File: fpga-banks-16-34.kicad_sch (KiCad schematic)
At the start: 22 parts, among them U3002 XC7K160T-FFG676, U9002 PCA9517A_TSSOP, Y9001 Oscillator_100MHz_ASFL1

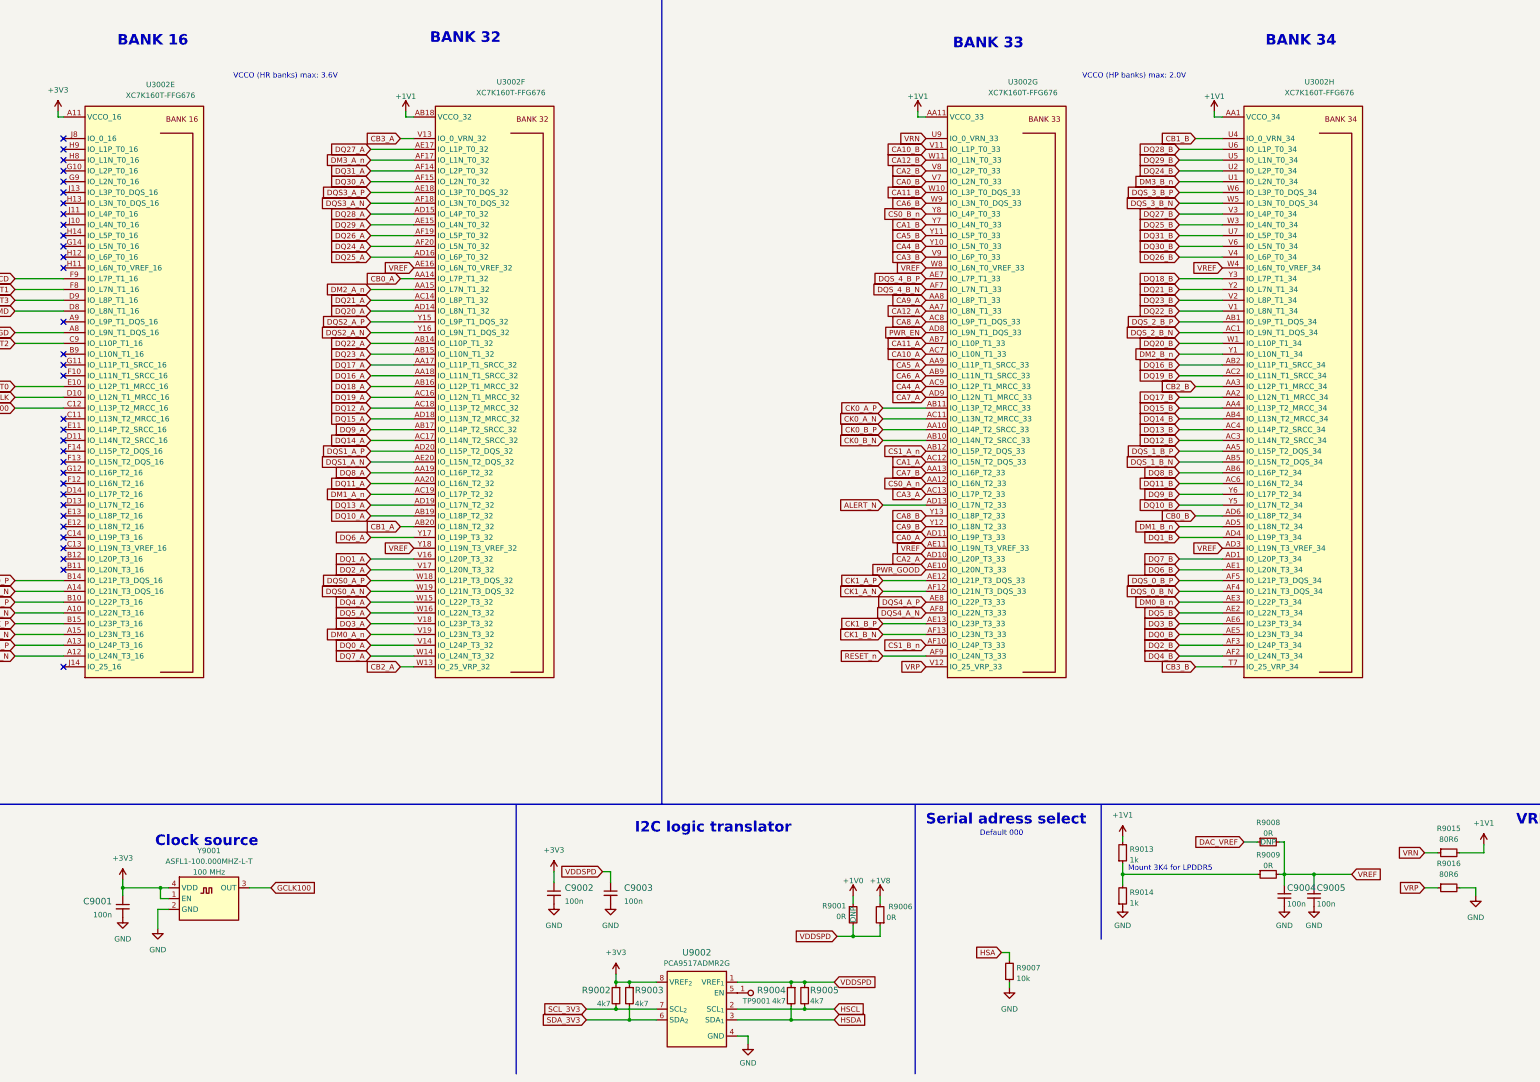
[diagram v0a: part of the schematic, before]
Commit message: Re-annotate schematic
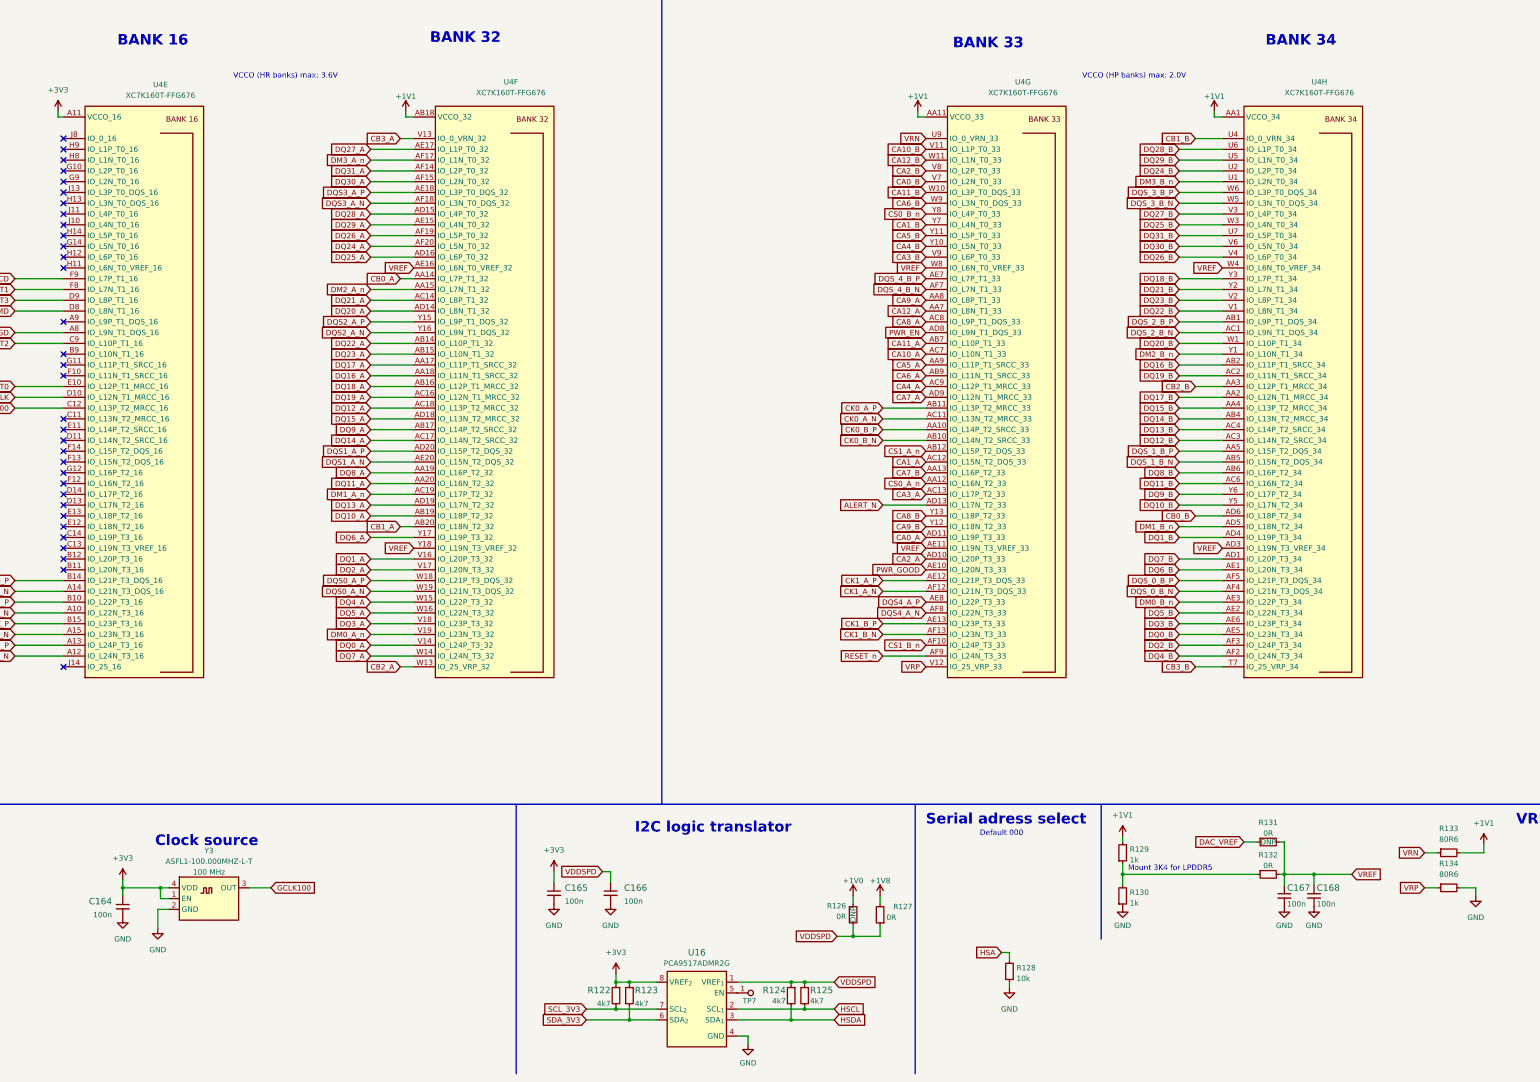
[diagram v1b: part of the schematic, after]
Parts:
- renumbered C9001 to C164, C9002 to C165, C9003 to C166, C9004 to C167, C9005 to C168, R9002 to R122, R9003 to R123, R9004 to R124, R9005 to R125, R9001 to R126, R9006 to R127, R9007 to R128, R9013 to R129, R9014 to R130, R9008 to R131, R9009 to R132, R9015 to R133, R9016 to R134, TP9001 to TP7, U9002 to U16, U3002 to U4, Y9001 to Y3

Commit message: Add local libraries
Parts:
- R129, R130: footprint antmicro-footprints:R_0402_1005Metric -> sodimm-ddr5-tester-footprints:R_0402_1005Metric; symbol antmicroResistors0402:R_1k_0402 -> sodimm-ddr5-tester:R_1k_0402
- R131, R132: footprint antmicro-footprints:R_0402_1005Metric -> sodimm-ddr5-tester-footprints:R_0402_1005Metric; symbol antmicroResistors0402:R_0R_0402 -> sodimm-ddr5-tester:R_0R_0402
- TP7: footprint antmicro-footprints:TP_SMD_1mm -> sodimm-ddr5-tester-footprints:TP_SMD_1mm; symbol antmicroTestPoints:TP_1mm_SMD -> sodimm-ddr5-tester:TP_1mm_SMD
- Y3: footprint antmicro-footprints:Oscillator_SMD_Abracon_ASFL1-4Pin_5.0x3.2mm -> sodimm-ddr5-tester-footprints:Oscillator_SMD_Abracon_ASFL1-4Pin_5.0x3.2mm; symbol antmicroOscillators:Oscillator_100MHz_ASFL1 -> sodimm-ddr5-tester:Oscillator_100MHz_ASFL1

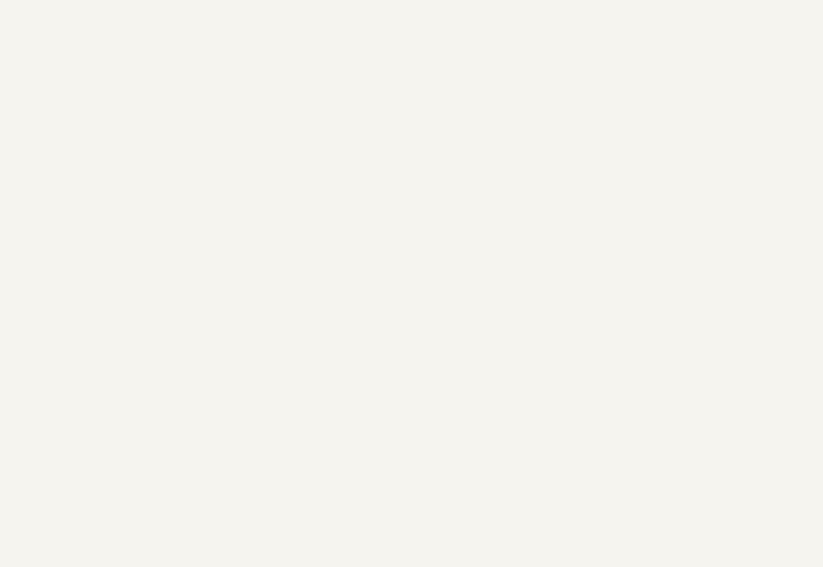
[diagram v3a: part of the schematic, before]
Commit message: Define DDR5, HyperBus and I2C buses. Connect HyperRAM with hierarchical bus
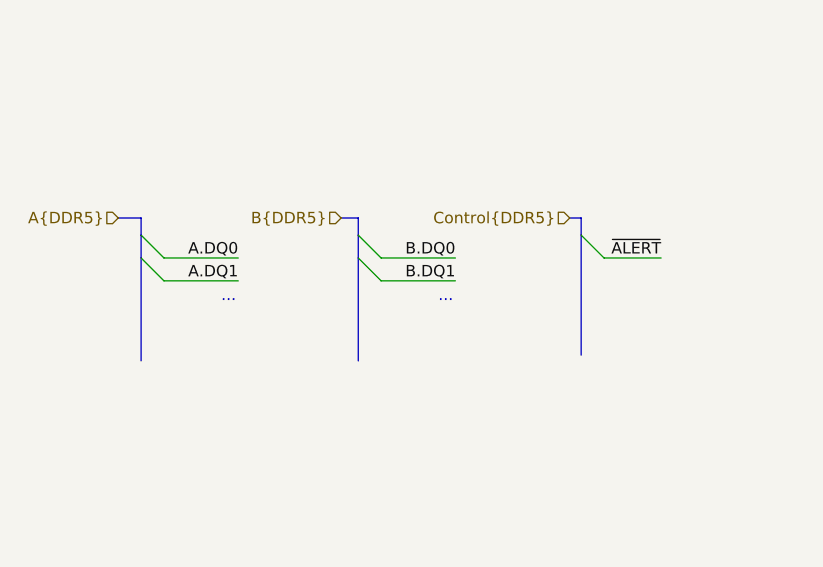
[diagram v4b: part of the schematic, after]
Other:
- note added: "..."
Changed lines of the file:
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@@
   (no_connect (at 55.88 80.01))
   (no_connect (at 55.88 148.59))
+  (bus_entry (at -13.97 136.525) (size 2.54 2.54)
+    (stroke (width 0) (type default) (color 0 0 0 0))
+  )
+  (bus_entry (at -62.865 136.525) (size 2.54 2.54)
+    (stroke (width 0) (type default) (color 0 0 0 0))
+  )
+  (bus_entry (at -38.735 136.525) (size 2.54 2.54)
+    (stroke (width 0) (type default) (color 0 0 0 0))
+  )
+  (bus_entry (at -62.865 139.065) (size 2.54 2.54)
+    (stroke (width 0) (type default) (color 0 0 0 0))
+  )
+  (bus_entry (at -38.735 139.065) (size 2.54 2.54)
+    (stroke (width 0) (type default) (color 0 0 0 0))
+  )
+  (bus (pts (xy -13.97 136.525) (xy -13.97 149.86))
+    (stroke (width 0) (type default) (color 0 0 0 0))
+  )
   (wire (pts (xy 128.27 87.63) (xy 138.43 87.63))
     (stroke (width 0) (type default) (color 0 0 0 0))
@@
     (stroke (width 0) (type default) (color 0 0 0 0))
   )
+  (bus (pts (xy -38.735 139.065) (xy -38.735 150.495))
+    (stroke (width 0) (type default) (color 0 0 0 0))
+  )
   (wire (pts (xy 384.81 241.3) (xy 388.62 241.3))
     (stroke (width 0) (type default) (color 0 0 0 0))
@@
     (stroke (width 0) (type default) (color 0 0 0 0))
   )
+  (bus (pts (xy -38.735 136.525) (xy -38.735 139.065))
+    (stroke (width 0) (type default) (color 0 0 0 0))
+  )
   (wire (pts (xy 318.77 82.55) (xy 328.93 82.55))
     (stroke (width 0) (type default) (color 0 0 0 0))
@@
     (stroke (width 0) (type default) (color 0 0 0 0))
   )
+  (bus (pts (xy -40.64 134.62) (xy -38.735 134.62))
+    (stroke (width 0) (type default) (color 0 0 0 0))
+  )
   (wire (pts (xy 44.45 128.27) (xy 55.88 128.27))
     (stroke (width 0) (type default) (color 0 0 0 0))
@@
     (stroke (width 0) (type default) (color 0 0 0 0))
   )
+  (wire (pts (xy -60.325 139.065) (xy -52.07 139.065))
+    (stroke (width 0) (type default) (color 0 0 0 0))
+  )
   (wire (pts (xy 138.43 151.13) (xy 128.27 151.13))
     (stroke (width 0) (type default) (color 0 0 0 0))
@@
     (stroke (width 0) (type default) (color 0 0 0 0))
   )
+  (bus (pts (xy -65.405 134.62) (xy -62.865 134.62))
+    (stroke (width 0) (type default) (color 0 0 0 0))
+  )
   (wire (pts (xy 318.77 148.59) (xy 328.93 148.59))
     (stroke (width 0) (type default) (color 0 0 0 0))
   )
+  (bus (pts (xy -13.97 134.62) (xy -13.97 136.525))
+    (stroke (width 0) (type default) (color 0 0 0 0))
+  )
   (wire (pts (xy 189.23 263.525) (xy 189.23 264.16))
     (stroke (width 0) (type default) (color 0 0 0 0))
@@
     (stroke (width 0) (type default) (color 0 0 0 0))
   )
+  (wire (pts (xy -11.43 139.065) (xy -5.08 139.065))
+    (stroke (width 0) (type default) (color 0 0 0 0))
+  )
   (wire (pts (xy 318.77 102.87) (xy 328.93 102.87))
     (stroke (width 0) (type default) (color 0 0 0 0))
@@
     (stroke (width 0) (type default) (color 0 0 0 0))
   )
+  (bus (pts (xy -62.865 134.62) (xy -62.865 136.525))
+    (stroke (width 0) (type default) (color 0 0 0 0))
+  )
   (wire (pts (xy 128.27 166.37) (xy 138.43 166.37))
     (stroke (width 0) (type default) (color 0 0 0 0))
@@
     (stroke (width 0) (type default) (color 0 0 0 0))
   )
+  (bus (pts (xy -62.865 136.525) (xy -62.865 139.065))
+    (stroke (width 0) (type default) (color 0 0 0 0))
+  )
   (wire (pts (xy 136.525 58.42) (xy 136.525 59.69))
     (stroke (width 0) (type default) (color 0 0 0 0))
@@
     (stroke (width 0) (type default) (color 0 0 0 0))
   )
+  (wire (pts (xy -60.325 141.605) (xy -52.07 141.605))
+    (stroke (width 0) (type default) (color 0 0 0 0))
+  )
   (wire (pts (xy 318.77 173.99) (xy 328.93 173.99))
     (stroke (width 0) (type default) (color 0 0 0 0))
@@
     (stroke (width 0) (type default) (color 0 0 0 0))
   )
+  (bus (pts (xy -38.735 134.62) (xy -38.735 136.525))
+    (stroke (width 0) (type default) (color 0 0 0 0))
+  )
   (wire (pts (xy 318.77 67.31) (xy 328.93 67.31))
     (stroke (width 0) (type default) (color 0 0 0 0))
@@
     (stroke (width 0) (type default) (color 0 0 0 0))
   )
+  (bus (pts (xy -15.24 134.62) (xy -13.97 134.62))
+    (stroke (width 0) (type default) (color 0 0 0 0))
+  )
+  (bus (pts (xy -62.865 139.065) (xy -62.865 150.495))
+    (stroke (width 0) (type default) (color 0 0 0 0))
+  )
   (wire (pts (xy 318.77 80.01) (xy 328.93 80.01))
     (stroke (width 0) (type default) (color 0 0 0 0))
   )
+  (wire (pts (xy -36.195 141.605) (xy -27.94 141.605))
+    (stroke (width 0) (type default) (color 0 0 0 0))
+  )
   (wire (pts (xy 128.27 82.55) (xy 138.43 82.55))
     (stroke (width 0) (type default) (color 0 0 0 0))
@@
     (stroke (width 0) (type default) (color 0 0 0 0))
   )
+  (wire (pts (xy -36.195 139.065) (xy -27.94 139.065))
+    (stroke (width 0) (type default) (color 0 0 0 0))
+  )
   (wire (pts (xy 69.85 241.3) (xy 78.74 241.3))
     (stroke (width 0) (type default) (color 0 0 0 0))
@@
     (effects (font (size 1.27 1.27)) (justify left bottom))
   )
+  (text "..." (at -29.845 144.145 0)
+    (effects (font (size 1.27 1.27)) (justify left bottom))
+  )
+  (text "..." (at -53.975 144.145 0)
+    (effects (font (size 1.27 1.27)) (justify left bottom))
+  )
   (text "VCCO (HP banks) max: 2.0V" (at 295.91 50.8 0)
     (effects (font (size 1.27 1.27)) (justify left bottom))
@@
     (effects (font (size 2.4892 2.4892) (thickness 0.4978) bold) (justify left bottom))
   )
+  (label "A.DQ0" (at -52.07 139.065 180)
+    (effects (font (size 1.27 1.27)) (justify right bottom))
+  )
+  (label "~{ALERT}" (at -5.08 139.065 180)
+    (effects (font (size 1.27 1.27)) (justify right bottom))
+  )
+  (label "A.DQ1" (at -52.07 141.605 180)
+    (effects (font (size 1.27 1.27)) (justify right bottom))
+  )
+  (label "B.DQ0" (at -27.94 139.065 180)
+    (effects (font (size 1.27 1.27)) (justify right bottom))
+  )
+  (label "B.DQ1" (at -27.94 141.605 180)
+    (effects (font (size 1.27 1.27)) (justify right bottom))
+  )
   (global_label "DQ20_B" (shape input) (at 318.77 113.03 180) (fields_autoplaced)
     (effects (font (size 1.27 1.27)) (justify right))
@@
     )
   )
+  (hierarchical_label "B{DDR5}" (shape input) (at -40.64 134.62 180)
+    (effects (font (size 1.27 1.27)) (justify right))
+  )
+  (hierarchical_label "A{DDR5}" (shape input) (at -65.405 134.62 180)
+    (effects (font (size 1.27 1.27)) (justify right))
+  )
+  (hierarchical_label "Control{DDR5}" (shape input) (at -15.24 134.62 180)
+    (effects (font (size 1.27 1.27)) (justify right))
+  )
   (symbol (lib_id "sodimm-ddr5-tester:PCA9517A_TSSOP") (at 214.63 263.525 0) (mirror y) (unit 1)

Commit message: Connect DDR hierarchical labels. Define and connect JTAG, RGMII, TDMS, UART, and SDIO buses. Reorganize schematic blocks between sheets
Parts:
- removed C165, C166: C_100n_0402, sodimm-ddr5-tester-footprints:C_0402_1005Metric, symbol sodimm-ddr5-tester:C_100n_0402
- removed R122, R123, R124, R125: R_4k7_0402, sodimm-ddr5-tester-footprints:R_0402_1005Metric, symbol sodimm-ddr5-tester:R_4k7_0402
- removed R126, R127: R_0R_0402, sodimm-ddr5-tester-footprints:R_0402_1005Metric, symbol sodimm-ddr5-tester:R_0R_0402
- removed R128: R_10k_0402, sodimm-ddr5-tester-footprints:R_0402_1005Metric, symbol sodimm-ddr5-tester:R_10k_0402
- removed TP7: TP_1mm_SMD, sodimm-ddr5-tester-footprints:TP_SMD_1mm, symbol sodimm-ddr5-tester:TP_1mm_SMD
- removed U16: PCA9517A_TSSOP, sodimm-ddr5-tester-footprints:TSSOP-8_3x3mm_P0.65mm, symbol sodimm-ddr5-tester:PCA9517A_TSSOP
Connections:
- net DQ0_A is gone; now on net A.DQ0: U4.V14 (IO_L24P_T3_32)
- net DQ0_B is gone; now on net B.DQ0: U4.AE5 (IO_L23N_T3_34)
- net DQ1_A is gone; now on net A.DQ1: U4.V16 (IO_L20P_T3_32)
- net DQ1_B is gone; now on net B.DQ1: U4.AD4 (IO_L19P_T3_34)
- net ALERT_N renamed Control.~{ALERT}
- net CA0_A renamed A.CA0
- net CA0_B renamed B.CA0
- net CA10_A renamed A.CA10
- net CA10_B renamed B.CA10
- net CA11_A renamed A.CA11
- net CA11_B renamed B.CA11
- net CA12_A renamed A.CA12
- net CA12_B renamed B.CA12
- net CA1_A renamed A.CA1
- net CA1_B renamed B.CA1
- net CA2_A renamed A.CA2
- net CA2_B renamed B.CA2
- net CA3_A renamed A.CA3
- net CA3_B renamed B.CA3
- net CA4_A renamed A.CA4
- net CA4_B renamed B.CA4
- net CA5_A renamed A.CA5
- net CA5_B renamed B.CA5
- net CA6_A renamed A.CA6
- net CA6_B renamed B.CA6
- net CA7_A renamed A.CA7
- net CA7_B renamed B.CA7
- net CA8_A renamed A.CA8
- net CA8_B renamed B.CA8
- net CA9_A renamed A.CA9
- net CA9_B renamed B.CA9
- net CB0_A renamed A.CB0
- net CB0_B renamed B.CB0
- net CB1_A renamed A.CB1
- net CB1_B renamed B.CB1
- net CB2_A renamed A.CB2
- net CB2_B renamed B.CB2
- net CB3_A renamed A.CB3
- net CB3_B renamed B.CB3
- net CK0_A_N renamed A.CK0_N
- net CK0_A_P renamed A.CK0_P
- net CK0_B_N renamed B.CK0_N
- net CK0_B_P renamed B.CK0_P
- net CK1_A_N renamed A.CK1_N
- net CK1_A_P renamed A.CK1_P
- net CK1_B_N renamed B.CK1_N
- net CK1_B_P renamed B.CK1_P
- net CS0_A_n renamed A.~{CS0}
- net CS0_B_n renamed B.~{CS0}
- net CS1_A_n renamed A.~{CS1}
- net CS1_B_n renamed B.~{CS1}
- net DM0_A_n renamed A.~{DM0}
- net DM0_B_n renamed B.~{DM0}
- net DM1_A_n renamed A.~{DM1}
- net DM1_B_n renamed B.~{DM1}
- net DM2_A_n renamed A.~{DM2}
- net DM2_B_n renamed B.~{DM2}
- net DM3_A_n renamed A.~{DM3}
- net DM3_B_n renamed B.~{DM3}
- net DQ10_A renamed A.DQ10
- net DQ10_B renamed B.DQ10
- net DQ11_A renamed A.DQ11
- net DQ11_B renamed B.DQ11
- net DQ12_A renamed A.DQ12
- net DQ12_B renamed B.DQ12
- net DQ13_A renamed A.DQ13
- net DQ13_B renamed B.DQ13
- net DQ14_A renamed A.DQ14
- net DQ14_B renamed B.DQ14
- net DQ15_A renamed A.DQ15
- net DQ15_B renamed B.DQ15
- net DQ16_A renamed A.DQ16
- net DQ16_B renamed B.DQ16
- net DQ17_A renamed A.DQ17
- net DQ17_B renamed B.DQ17
- net DQ18_A renamed A.DQ18
- net DQ18_B renamed B.DQ18
- net DQ19_A renamed A.DQ19
- net DQ19_B renamed B.DQ19
- net DQ20_A renamed A.DQ20
- net DQ20_B renamed B.DQ20
- net DQ21_A renamed A.DQ21
- net DQ21_B renamed B.DQ21
- net DQ22_A renamed A.DQ22
- net DQ22_B renamed B.DQ22
- net DQ23_A renamed A.DQ23
- net DQ23_B renamed B.DQ23
- net DQ24_A renamed A.DQ24
- net DQ24_B renamed B.DQ24
- net DQ25_A renamed A.DQ25
- net DQ25_B renamed B.DQ25
- net DQ26_A renamed A.DQ26
- net DQ26_B renamed B.DQ26
- net DQ27_A renamed A.DQ27
- net DQ27_B renamed B.DQ27
- net DQ28_A renamed A.DQ28
- net DQ28_B renamed B.DQ28
- net DQ29_A renamed A.DQ29
- net DQ29_B renamed B.DQ29
- net DQ2_A renamed A.DQ2
- net DQ2_B renamed B.DQ2
- net DQ30_A renamed A.DQ30
- net DQ30_B renamed B.DQ30
- net DQ31_A renamed A.DQ31
- net DQ31_B renamed B.DQ31
- net DQ3_A renamed A.DQ3
- net DQ3_B renamed B.DQ3
- net DQ4_A renamed A.DQ4
- net DQ4_B renamed B.DQ4
- net DQ5_A renamed A.DQ5
- net DQ5_B renamed B.DQ5
- net DQ6_A renamed A.DQ6
- net DQ6_B renamed B.DQ6
- net DQ7_A renamed A.DQ7
- net DQ7_B renamed B.DQ7
- net DQ8_A renamed A.DQ8
- net DQ8_B renamed B.DQ8
- net DQ9_A renamed A.DQ9
- net DQ9_B renamed B.DQ9
- net DQS0_A_N renamed A.DQS0_N
- net DQS0_A_P renamed A.DQS0_P
- net DQS1_A_N renamed A.DQS1_N
- net DQS1_A_P renamed A.DQS1_P
- net DQS2_A_N renamed A.DQS2_N
- net DQS2_A_P renamed A.DQS2_P
- net DQS3_A_N renamed A.DQS3_N
- net DQS3_A_P renamed A.DQS3_P
- net DQS4_A_N renamed A.DQS4_N
- net DQS4_A_P renamed A.DQS4_P
- net DQS_0_B_N renamed B.DQS0_N
- net DQS_0_B_P renamed B.DQS0_P
- net DQS_1_B_N renamed B.DQS1_N
- net DQS_1_B_P renamed B.DQS1_P
- net DQS_2_B_N renamed B.DQS2_N
- net DQS_2_B_P renamed B.DQS2_P
- net DQS_3_B_N renamed B.DQS3_N
- net DQS_3_B_P renamed B.DQS3_P
- net DQS_4_B_N renamed B.DQS4_N
- net DQS_4_B_P renamed B.DQS4_P
- net PWR_EN renamed Control.PWR_EN
- net PWR_GOOD renamed Control.PWR_GOOD
- net RESET_n renamed Control.~{RESET}
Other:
- note removed: "..."
- note removed: "Default 000"
- note removed: "Serial adress select"
- moved on the sheet: U4F, U4G, U4H
